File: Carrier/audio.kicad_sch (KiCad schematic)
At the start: 6 parts, among them U6 MAX98357A

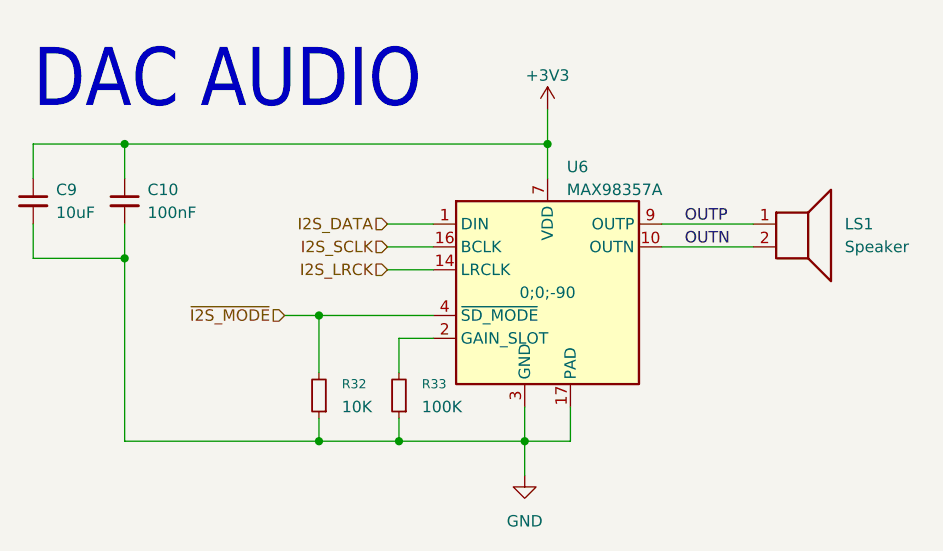
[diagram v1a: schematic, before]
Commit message: fix: speaker connector from SH-1.0 to PH-2.0
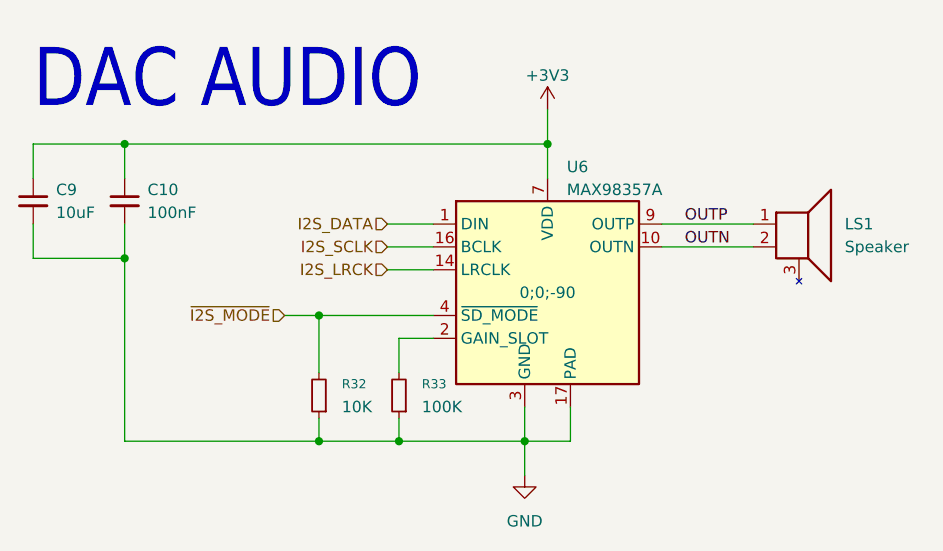
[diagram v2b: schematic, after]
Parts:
- LS1: footprint Connector_JST:JST_SH_SM02B-SRSS-TB_1x02-1MP_P1.00mm_Horizontal -> badge:JST_PH_S2B-PH-K_1x02_P2.00mm_Horizontal; symbol Device:Speaker -> badge_why2025:Speaker
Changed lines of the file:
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@@
 	)
 	(symbol
-		(lib_id "Device:Speaker")
+		(lib_id "badge_why2025:Speaker")
 		(at 137.16 60.96 0)
 		(unit 1)
@@
 			)
 		)
-		(property "Footprint" "Connector_JST:JST_SH_SM02B-SRSS-TB_1x02-1MP_P1.00mm_Horizontal"
+		(property "Footprint" "badge:JST_PH_S2B-PH-K_1x02_P2.00mm_Horizontal"
 			(at 137.16 66.04 0)
 			(effects
@@
 		(pin "1"
 		)
+		(pin "3"
+		)
 		(instances

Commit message: Moved lcd screen connector for new screen, corrected LCSC partnumbers
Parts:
- LS1: footprint badge:JST_PH_S2B-PH-K_1x02_P2.00mm_Horizontal -> Connector_JST:JST_PH_S2B-PH-SM4-TB_1x02-1MP_P2.00mm_Horizontal; LCSC C160402 -> C295747
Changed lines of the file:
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@@
 			)
 		)
-		(property "Footprint" "badge:JST_PH_S2B-PH-K_1x02_P2.00mm_Horizontal"
+		(property "Footprint" "Connector_JST:JST_PH_S2B-PH-SM4-TB_1x02-1MP_P2.00mm_Horizontal"
 			(at 137.16 66.04 0)
 			(effects
@@
 			)
 		)
-		(property "LCSC" "C160402"
+		(property "LCSC" "C295747"
 			(at 137.16 60.96 0)
 			(effects
